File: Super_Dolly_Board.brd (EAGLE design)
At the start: 154.5 x 45.8 mm, 109 parts, among them J1 10118193-0001LF, J3 SJ1-2503A, J4 RJHSE-5381, J5 SJ1-2503A, J6 SJ1-2503A, P1 TC33X-2, SW1 SKQUDBE010, U1 AT90USB646-MU, U10 IP4234CZ6, U11 AT90USB646-AU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

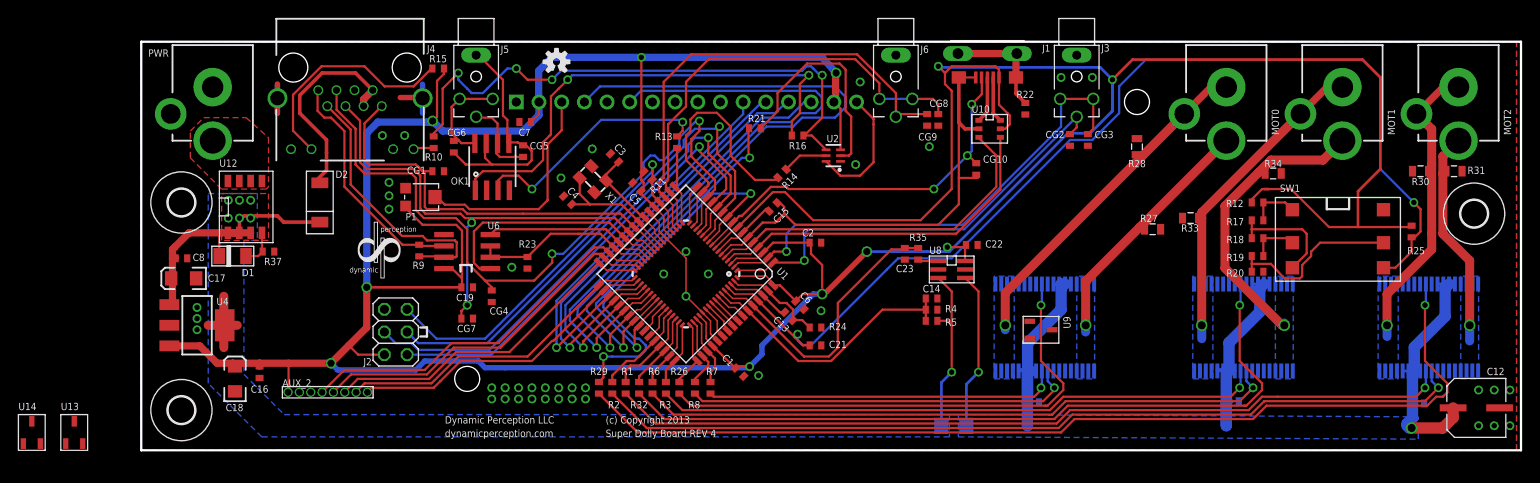
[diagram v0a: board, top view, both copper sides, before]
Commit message: REV4 of SDB complete. added 2 parts to datasheets and libraires.
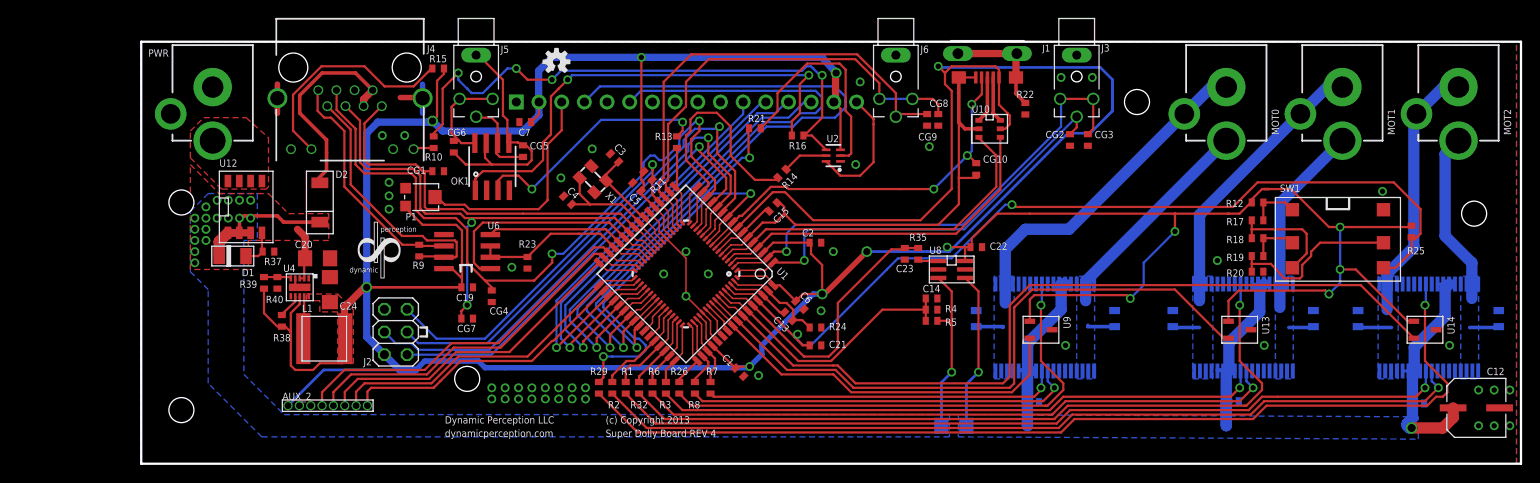
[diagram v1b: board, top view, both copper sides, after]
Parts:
- removed C16: .1uF, parkers_parts:0402_CAP
- removed C17: 2.2uF, SparkFun:EIA3216
- removed C18: 10uF, SparkFun:EIA3216
- removed C8: .1uF 35V, parkers_parts:0402_CAP
- removed H1, H2, H4: MOUNT-HOLE3.0, holes:3,0
- added C20: GRM32ER72A225KA35L, PP_Passives:1206
- added C24: C3225X5R1A226M, PP_Passives:1206
- added L1: SRN5020-100M, PP_Passives:SRN5020
- added R38: 100K, PP_Passives:0402
- added R39: 787K, PP_Passives:0402
- added R40: 150K, PP_Passives:0402
- U12: value BSO080P03NS3E G -> FDS6681Z
- U4: value TS2937CW50 -> (none); device SparkFun-PowerIC:SOT223 -> PP_DigitalIC:WSON-10
- moved U14 156.4 mm to (69.8, -13.2), turned to 270 degrees
- moved U13 131.0 mm to (49.0, -13.2), turned to 270 degrees
- moved R28 26.4 mm to (19.5, -12.0), flipped to the bottom
- moved R30 17.9 mm to (62.3, -12.0), flipped to the bottom, turned to 90 degrees
- moved R31 17.2 mm to (78.0, -12.0), flipped to the bottom, turned to 90 degrees
- moved R34 16.9 mm to (57.3, -12.0), flipped to the bottom, turned to 90 degrees
- moved U4 12.3 mm to (-56.3, -8.50), turned to 180 degrees
- moved R33 11.4 mm to (41.5, -12.0), flipped to the bottom, turned to 90 degrees
- moved R27 10.9 mm to (35.0, -12.0), flipped to the bottom, turned to 90 degrees
- moved AUX_2 1.50 mm to (-53.8, -21.8)
- moved C22 0.56 mm to (19.5, -4.00)
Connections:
- new net N$11: R38.1, U4.7
- new net N$13: L1.P$1, U4.9
- new net N$14: R39.1, R40.1, U4.5
- net +5V: now also C24.1, L1.P$2, R38.2, R39.2, U4.10, U4.8; no longer C16.1, C18.A, U4.3
- net GND: now also C20.2, C24.2, R40.2, U4.1, U4.4, U4.6, U4.PAD; no longer C16.2, C17.C, C18.C, C8.2, U4.2
- net VIN: now also C20.1, U4.2, U4.3; no longer C17.A, C8.1, U4.1
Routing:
- net TEMP2_SENSOR: track 3.69 -> 93.7 mm
- net TEMP1_SENSOR: track 3.54 -> 73.4 mm
- net +5V: track 491.5 -> 545.5 mm, vias 11 -> 14
- net TEMP0_SENSOR: track 3.54 -> 44.8 mm
- net BTNS: track 120.3 -> 101.9 mm
- net M1_O1: track 33.7 -> 24.4 mm, vias 1 -> 0
- net GND: track 39.6 -> 31.6 mm, vias 44 -> 47
- net VIN: track 51.8 -> 44.5 mm, vias 7 -> 18
- net N$13: track 0.00 -> 4.79 mm
- net N$14: track 0.00 -> 3.06 mm
- net M0_O2: track 39.0 -> 41.9 mm, vias 1 -> 0
- net N$11: track 0.00 -> 2.75 mm
- net M2_O1: track 25.0 -> 22.8 mm, vias 1 -> 0
- net PE1: track 35.5 -> 37.0 mm
- net PE0: track 36.6 -> 38.1 mm
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- added copper zone on layer 1, net +5V
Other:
- board size 154.5 x 45.8 mm -> 154.5 x 47.2 mm

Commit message: added a part to PP_poweric and replaced the switcher regulator with a linear one.
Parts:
- removed C20: GRM32ER72A225KA35L, PP_Passives:1206
- removed C24: C3225X5R1A226M, PP_Passives:1206
- removed L1: SRN5020-100M, PP_Passives:SRN5020
- removed R38: 100K, PP_Passives:0402
- removed R39: 787K, PP_Passives:0402
- removed R40: 150K, PP_Passives:0402
- added C16: .1uF, parkers_parts:0402_CAP
- added C17: 2.2uF, SparkFun:EIA3216
- added C18: 10uF, SparkFun:EIA3216
- added C8: .1uF 35V, parkers_parts:0402_CAP
- U4: value (none) -> MC78M05CDTG; device PP_DigitalIC:WSON-10 -> PP_PowerIC:DPAK-3
- moved U4 11.7 mm to (-66.8, -13.8)
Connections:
- removed net N$11: R38.1, U4.7
- removed net N$13: L1.P$1, U4.9
- removed net N$14: R39.1, R40.1, U4.5
- net +5V: now also C16.1, C18.A, U4.2; no longer C24.1, L1.P$2, R38.2, R39.2, U4.10, U4.8
- net GND: now also C16.2, C17.C, C18.C, C8.2; no longer C20.2, C24.2, R40.2, U4.1, U4.6, U4.PAD
- net UGND: no longer CG10.1
- net VIN: now also C17.A, C8.1, U4.1; no longer C20.1, U4.2, U4.3
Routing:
- net N$13: track 4.79 -> 0.00 mm
- net +5V: track 545.5 -> 550.1 mm
- net VIN: track 44.5 -> 47.6 mm
- net N$14: track 3.06 -> 0.00 mm
- net N$11: track 2.75 -> 0.00 mm
- net GND: track 31.6 -> 30.6 mm, vias 47 -> 59
- removed copper zone on layer 1, net +5V

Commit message: changed ESD protection to TPD1E10B06DPYR
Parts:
- CG1, CG10, CG2, CG3, CG4, CG5, CG6, CG7, CG8, CG9: value CG0402MLC-05LG -> TPD1E10B06DPYR
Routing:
- net +5V: track 550.1 -> 537.7 mm
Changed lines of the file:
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@@
 <attribute name="NAME" x="33.5" y="17.9" size="0.8128" layer="25" font="vector"/>
 </element>
-<element name="CG2" library="parkers_parts" package="0402_RES" value="CG0402MLC-05LG" x="30" y="8" smashed="yes" rot="R90">
+<element name="CG2" library="parkers_parts" package="0402_RES" value="TPD1E10B06DPYR" x="30" y="8" smashed="yes" rot="R90">
 <attribute name="NAME" x="27.261" y="8.1985" size="0.8128" layer="25" font="vector"/>
 </element>
-<element name="CG3" library="parkers_parts" package="0402_RES" value="CG0402MLC-05LG" x="32" y="8" smashed="yes" rot="R90">
+<element name="CG3" library="parkers_parts" package="0402_RES" value="TPD1E10B06DPYR" x="32" y="8" smashed="yes" rot="R90">
 <attribute name="NAME" x="32.761" y="8.1985" size="0.8128" layer="25" font="vector"/>
 </element>
@@
 <attribute name="NAME" x="3.011" y="-15.3015" size="0.8128" layer="25" font="vector"/>
 </element>
-<element name="CG5" library="parkers_parts" package="0402_RES" value="CG0402MLC-05LG" x="-31.25" y="6.75" smashed="yes" rot="R270">
+<element name="CG5" library="parkers_parts" package="0402_RES" value="TPD1E10B06DPYR" x="-31.25" y="6.75" smashed="yes" rot="R270">
 <attribute name="NAME" x="-30.489" y="6.9485" size="0.8128" layer="25" font="vector"/>
 </element>
-<element name="CG6" library="parkers_parts" package="0402_RES" value="CG0402MLC-05LG" x="-39" y="7.25" smashed="yes" rot="R90">
+<element name="CG6" library="parkers_parts" package="0402_RES" value="TPD1E10B06DPYR" x="-39" y="7.25" smashed="yes" rot="R90">
 <attribute name="NAME" x="-39.739" y="8.4485" size="0.8128" layer="25" font="vector"/>
 </element>
@@
 <attribute name="NAME" x="-52.25" y="3.75" size="0.8128" layer="25" font="vector"/>
 </element>
-<element name="CG4" library="parkers_parts" package="0402_RES" value="CG0402MLC-05LG" x="-34.75" y="-9.5" smashed="yes" rot="R270">
+<element name="CG4" library="parkers_parts" package="0402_RES" value="TPD1E10B06DPYR" x="-34.75" y="-9.5" smashed="yes" rot="R270">
 <attribute name="NAME" x="-34.989" y="-11.5515" size="0.8128" layer="25" font="vector"/>
 </element>
-<element name="CG7" library="parkers_parts" package="0402_RES" value="CG0402MLC-05LG" x="-37.5" y="-12" smashed="yes">
+<element name="CG7" library="parkers_parts" package="0402_RES" value="TPD1E10B06DPYR" x="-37.5" y="-12" smashed="yes">
 <attribute name="NAME" x="-36.511" y="-12.6985" size="0.8128" layer="25" font="vector" rot="R180"/>
 </element>
 <element name="U10" library="parkers_parts" package="SOT-457" value="IP4234CZ6" x="21" y="9.25"/>
-<element name="CG1" library="parkers_parts" package="0402_RES" value="CG0402MLC-05LG" x="-40.75" y="4.5" smashed="yes" rot="R180">
+<element name="CG1" library="parkers_parts" package="0402_RES" value="TPD1E10B06DPYR" x="-40.75" y="4.5" smashed="yes" rot="R180">
 <attribute name="NAME" x="-44.239" y="4.1985" size="0.8128" layer="25" font="vector"/>
 </element>
@@
 <attribute name="NAME" x="13.25" y="17.75" size="0.8128" layer="25" font="vector"/>
 </element>
-<element name="CG8" library="parkers_parts" package="0402_RES" value="CG0402MLC-05LG" x="15.249996875" y="10.250003125" smashed="yes" rot="R90">
+<element name="CG8" library="parkers_parts" package="0402_RES" value="TPD1E10B06DPYR" x="15.249996875" y="10.250003125" smashed="yes" rot="R90">
 <attribute name="NAME" x="14.261003125" y="11.698503125" size="0.8128" layer="25" font="vector"/>
 </element>
-<element name="CG9" library="parkers_parts" package="0402_RES" value="CG0402MLC-05LG" x="13.999996875" y="10.250003125" smashed="yes" rot="R90">
+<element name="CG9" library="parkers_parts" package="0402_RES" value="TPD1E10B06DPYR" x="13.999996875" y="10.250003125" smashed="yes" rot="R90">
 <attribute name="NAME" x="13.011003125" y="7.948503125" size="0.8128" layer="25" font="vector"/>
 </element>
@@
 <attribute name="NAME" x="58.48900625" y="-14.5515" size="0.8128" layer="26" font="vector" rot="MR0"/>
 </element>
-<element name="CG10" library="parkers_parts" package="0402_RES" value="CG0402MLC-05LG" x="19.5" y="4.75" smashed="yes" rot="R90">
+<element name="CG10" library="parkers_parts" package="0402_RES" value="TPD1E10B06DPYR" x="19.5" y="4.75" smashed="yes" rot="R90">
 <attribute name="NAME" x="20.261" y="5.4485" size="0.8128" layer="25" font="vector"/>
 </element>
@@
 <wire x1="-51.250003125" y1="-10.75" x2="-49.000003125" y2="-8.5" width="0.8128" layer="1"/>
 <wire x1="-49.000003125" y1="-8.5" x2="-48.749996875" y2="-8.5" width="0.8128" layer="1"/>
-<wire x1="-57.560003125" y1="-21.75" x2="-53.560003125" y2="-17.75" width="0.3048" layer="16"/>
-<wire x1="-53.560003125" y1="-17.75" x2="-45.06" y2="-17.75" width="0.3048" layer="16"/>
 <contactref element="C16" pad="1"/>
 <contactref element="C18" pad="A"/>
@@
 <wire x1="-65.400003125" y1="-21.5" x2="-60.250003125" y2="-21.5" width="0.8128" layer="1"/>
 <wire x1="-60.250003125" y1="-21.5" x2="-58.845003125" y2="-20.095" width="0.8128" layer="1"/>
-<wire x1="-58.845003125" y1="-20.095" x2="-55.905003125" y2="-20.095" width="0.8128" layer="1"/>
+<wire x1="-58.845003125" y1="-20.095" x2="-57.500003125" y2="-20.095" width="0.8128" layer="1"/>
+<wire x1="-57.500003125" y1="-20.095" x2="-55.905003125" y2="-20.095" width="0.8128" layer="1"/>
 <wire x1="-55.905003125" y1="-20.095" x2="-51.250003125" y2="-15.44" width="0.8128" layer="1"/>
 <wire x1="-51.250003125" y1="-15.44" x2="-51.250003125" y2="-14.15" width="0.8128" layer="1"/>
+<wire x1="-57.560003125" y1="-21.75" x2="-57.500003125" y2="-21.75" width="0.4064" layer="1"/>
+<wire x1="-57.500003125" y1="-21.75" x2="-57.500003125" y2="-20.095" width="0.4064" layer="1"/>
 </signal>
 <signal name="GND">

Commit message: added input board
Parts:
- removed SW1: SKQUDBE010, parkers_parts:APLS_SKQ_MDS_SMD
- added J7: HFW6R-2STE1LF, PP_Connectors:HFW6R-2STE1LF
- moved R25 18.1 mm to (51.0, 3.25), turned to 180 degrees
- moved R17 2.00 mm to (51.0, -3.00), turned to 180 degrees
- moved R18 2.00 mm to (51.0, -1.00)
- turned R19 to 0 degrees
- turned R20 to 180 degrees
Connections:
- net BTNS: now also J7.2; no longer SW1.4
- net GND: now also J7.1; no longer SW1.6
- net N$27: now also J7.6, R18.2; no longer R17.2, SW1.1
- net N$28: now also J7.4, R19.1; no longer R18.2, SW1.3
- net N$29: now also J7.5, R17.2; no longer R19.1, SW1.2
- net N$30: now also J7.3; no longer SW1.5
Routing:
- net N$30: track 19.9 -> 6.81 mm
- net BTNS: track 101.9 -> 95.9 mm
- net +5V: track 537.7 -> 531.8 mm
- net N$28: track 12.8 -> 7.06 mm
- net N$27: track 5.59 -> 6.97 mm
- net N$29: track 5.46 -> 6.56 mm
- net GND: vias 59 -> 58

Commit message: fixed a part number issue
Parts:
- U8: value LMP8640MK-H/NOPB -> LMP8640MK-F/NOPB
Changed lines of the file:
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@@
 </element>
 <element name="AUX_2" library="PP_Connectors" package="HEADER_01X08_1.27_PTH" value="" x="-53.750003125" y="-21.75"/>
-<element name="U8" library="PP_AnalogIC" package="TSOT-6" value="LMP8640MK-H/NOPB" x="16.75" y="-6.5" smashed="yes" rot="R270">
+<element name="U8" library="PP_AnalogIC" package="TSOT-6" value="LMP8640MK-F/NOPB" x="16.75" y="-6.5" smashed="yes" rot="R270">
 <attribute name="NAME" x="14.25" y="-4.75" size="0.8128" layer="21" font="vector"/>
 </element>

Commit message: Fixed some small isues with the SDM REV4 and tagged it as REV5. Added the spreadsheet BOM.
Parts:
- added U15: MC78M05CDTG, PP_PowerIC:DPAK-3
- CG1, CG10, CG2, CG3, CG4, CG5, CG6, CG7, CG8, CG9: value TPD1E10B06DPYR -> CG0402MLC-05LG
- moved LOGO2 114.3 mm to (64.5, -5.25)
- moved D2 2.14 mm to (-54.8, 3.00), turned to 0 degrees
- moved C18 1.50 mm to (-64.8, -19.2)
- renumbered C23 to C20
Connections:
- new net 12VB_D: D2.CATHODE, U15.1
- net +5V: now also U15.2
- net GND: now also U15.4
- net VIN: no longer D2.CATHODE
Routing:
- net VIN: track 47.6 -> 29.8 mm, vias 18 -> 24
- net 12VB_D: track 0.00 -> 6.25 mm
- net +5V: track 531.8 -> 536.5 mm
- net 12VB: track 24.5 -> 23.7 mm
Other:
- board text added: "LCD1"
